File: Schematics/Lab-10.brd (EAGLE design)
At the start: 160 x 100 mm, 15 parts, among them IC1 OP350N, Q1 IRLD024

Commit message: Added LCD interface to the schematic
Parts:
- added C3: 0.33uf, EE445L:CAP100MIL
- added U$2: ST7735, EE445L:ST7735
- C2: value (none) -> 0.1uf
- R3, R4, R5, R6, R7: value (none) -> 10k
- R8: value (none) -> 200k
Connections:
- new net CS: U$1.J2-12, U$2.6
- new net D?C: U$1.J1-9, U$2.4
- new net MISO: U$1.J2-13, U$2.9
- new net MOSI: U$1.J1-8, U$2.7
- new net N$3: C3.2, Q1.P$3
- new net RST: U$1.J1-10, U$2.3
- new net SCK: U$1.J2-11, U$2.8
- net +3V3: now also U$2.10, U$2.2
- net GND: now also U$2.1
- net N$1: now also C3.1; no longer Q1.P$3
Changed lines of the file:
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@@
 <attribute name="VALUE" x="-61.976" y="-6.477" size="1.27" layer="27" ratio="10"/>
 </element>
-<element name="R3" library="EE445L" package="RES300MIL" value="" x="-59.69" y="-10.16" smashed="yes">
+<element name="R3" library="EE445L" package="RES300MIL" value="10k" x="-59.69" y="-10.16" smashed="yes">
 <attribute name="NAME" x="-62.23" y="-8.8646" size="0.9906" layer="25" ratio="10"/>
 <attribute name="VALUE" x="-61.3156" y="-10.6426" size="0.9906" layer="27" ratio="10"/>
 </element>
-<element name="R4" library="EE445L" package="RES300MIL" value="" x="-59.69" y="-15.24" smashed="yes">
+<element name="R4" library="EE445L" package="RES300MIL" value="10k" x="-59.69" y="-15.24" smashed="yes">
 <attribute name="NAME" x="-62.23" y="-13.9446" size="0.9906" layer="25" ratio="10"/>
 <attribute name="VALUE" x="-61.3156" y="-15.7226" size="0.9906" layer="27" ratio="10"/>
@@
 <attribute name="VALUE" x="-60.706" y="-22.225" size="1.27" layer="27" ratio="10"/>
 </element>
-<element name="R5" library="EE445L" package="RES200MIL" value="" x="-60.96" y="-29.21" smashed="yes">
+<element name="R5" library="EE445L" package="RES200MIL" value="10k" x="-60.96" y="-29.21" smashed="yes">
 <attribute name="NAME" x="-62.9666" y="-28.0416" size="0.9906" layer="25" ratio="10"/>
 <attribute name="VALUE" x="-63.0936" y="-31.5214" size="0.9906" layer="27" ratio="10"/>
 </element>
-<element name="R6" library="EE445L" package="RES200MIL" value="" x="-60.96" y="-33.02" smashed="yes">
+<element name="R6" library="EE445L" package="RES200MIL" value="10k" x="-60.96" y="-33.02" smashed="yes">
 <attribute name="NAME" x="-62.9666" y="-31.8516" size="0.9906" layer="25" ratio="10"/>
 <attribute name="VALUE" x="-63.0936" y="-35.3314" size="0.9906" layer="27" ratio="10"/>
 </element>
-<element name="R7" library="EE445L" package="RES200MIL" value="" x="-60.96" y="-36.83" smashed="yes">
+<element name="R7" library="EE445L" package="RES200MIL" value="10k" x="-60.96" y="-36.83" smashed="yes">
 <attribute name="NAME" x="-62.9666" y="-35.6616" size="0.9906" layer="25" ratio="10"/>
 <attribute name="VALUE" x="-63.0936" y="-39.1414" size="0.9906" layer="27" ratio="10"/>
 </element>
-<element name="R8" library="EE445L" package="RES200MIL" value="" x="-60.96" y="-40.64" smashed="yes">
+<element name="R8" library="EE445L" package="RES200MIL" value="200k" x="-60.96" y="-40.64" smashed="yes">
 <attribute name="NAME" x="-62.9666" y="-39.4716" size="0.9906" layer="25" ratio="10"/>
 <attribute name="VALUE" x="-63.0936" y="-42.9514" size="0.9906" layer="27" ratio="10"/>
 </element>
-<element name="C2" library="EE445L" package="CAP100MIL" value="" x="-62.23" y="-45.72" smashed="yes">
+<element name="C2" library="EE445L" package="CAP100MIL" value="0.1uf" x="-62.23" y="-45.72" smashed="yes">
 <attribute name="NAME" x="-64.008" y="-44.323" size="1.27" layer="25" ratio="10"/>
 <attribute name="VALUE" x="-64.008" y="-48.387" size="1.27" layer="27" ratio="10"/>
 </element>
+<element name="C3" library="EE445L" package="CAP100MIL" value="0.33uf" x="-62.23" y="-53.34" smashed="yes">
+<attribute name="NAME" x="-64.008" y="-51.943" size="1.27" layer="25" ratio="10"/>
+<attribute name="VALUE" x="-64.008" y="-56.007" size="1.27" layer="27" ratio="10"/>
+</element>
+<element name="U$2" library="EE445L" package="ST7735" value="ST7735" x="-62.23" y="-63.5" smashed="yes"/>
 </elements>
 <signals>
@@
 <contactref element="C2" pad="1"/>
 <contactref element="R5" pad="2"/>
+<contactref element="U$2" pad="1"/>
+<wire x1="-63.5" y1="-45.72" x2="-62.23" y2="-63.5" width="0" layer="19" extent="1-1"/>
 <wire x1="-58.42" y1="-29.21" x2="-63.5" y2="-45.72" width="0" layer="19" extent="1-1"/>
 <wire x1="-58.42" y1="-17.78" x2="-58.42" y2="-29.21" width="0" layer="19" extent="1-1"/>
@@
 <contactref element="C2" pad="2"/>
 <contactref element="R6" pad="1"/>
+<contactref element="U$2" pad="2"/>
+<contactref element="U$2" pad="10"/>
+<wire x1="-62.23" y1="-66.04" x2="-62.23" y2="-86.36" width="0" layer="19" extent="1-1"/>
+<wire x1="-60.96" y1="-45.72" x2="-62.23" y2="-66.04" width="0" layer="19" extent="1-1"/>
 <wire x1="-63.5" y1="-33.02" x2="-60.96" y2="-45.72" width="0" layer="19" extent="1-1"/>
 <wire x1="-53.34" y1="-25.4" x2="-63.5" y2="-33.02" width="0" layer="19" extent="1-1"/>
@@
 <signal name="N$1">
 <contactref element="R1" pad="2"/>
-<contactref element="Q1" pad="P$3"/>
-<wire x1="-49.53" y1="71.12" x2="-16.51" y2="71.12" width="0" layer="19" extent="1-1"/>
+<contactref element="C3" pad="1"/>
+<wire x1="-49.53" y1="71.12" x2="-63.5" y2="-53.34" width="0" layer="19" extent="1-1"/>
 </signal>
 <signal name="+5V">
@@
 <wire x1="-55.88" y1="-25.4" x2="-63.5" y2="-36.83" width="0" layer="19" extent="1-1"/>
 </signal>
+<signal name="N$3">
+<contactref element="Q1" pad="P$3"/>
+<contactref element="C3" pad="2"/>
+<wire x1="-16.51" y1="71.12" x2="-60.96" y2="-53.34" width="0" layer="19" extent="1-1"/>
+</signal>
+<signal name="RST">
+<contactref element="U$1" pad="J1-10"/>
+<contactref element="U$2" pad="3"/>
+<wire x1="-62.23" y1="13.97" x2="-62.23" y2="-68.58" width="0" layer="19" extent="1-1"/>
+</signal>
+<signal name="D?C">
+<contactref element="U$1" pad="J1-9"/>
+<contactref element="U$2" pad="4"/>
+<wire x1="-62.23" y1="16.51" x2="-62.23" y2="-71.12" width="0" layer="19" extent="1-1"/>
+</signal>
+<signal name="MOSI">
+<contactref element="U$1" pad="J1-8"/>
+<contactref element="U$2" pad="7"/>
+<wire x1="-62.23" y1="19.05" x2="-62.23" y2="-78.74" width="0" layer="19" extent="1-1"/>
+</signal>
+<signal name="MISO">
+<contactref element="U$1" pad="J2-13"/>
+<contactref element="U$2" pad="9"/>
+<wire x1="-16.51" y1="19.05" x2="-62.23" y2="-83.82" width="0" layer="19" extent="1-1"/>
+</signal>
+<signal name="CS">
+<contactref element="U$1" pad="J2-12"/>
+<contactref element="U$2" pad="6"/>
+<wire x1="-16.51" y1="16.51" x2="-62.23" y2="-76.2" width="0" layer="19" extent="1-1"/>
+</signal>
+<signal name="SCK">
+<contactref element="U$1" pad="J2-11"/>
+<contactref element="U$2" pad="8"/>
+<wire x1="-16.51" y1="13.97" x2="-62.23" y2="-81.28" width="0" layer="19" extent="1-1"/>
+</signal>
 </signals>

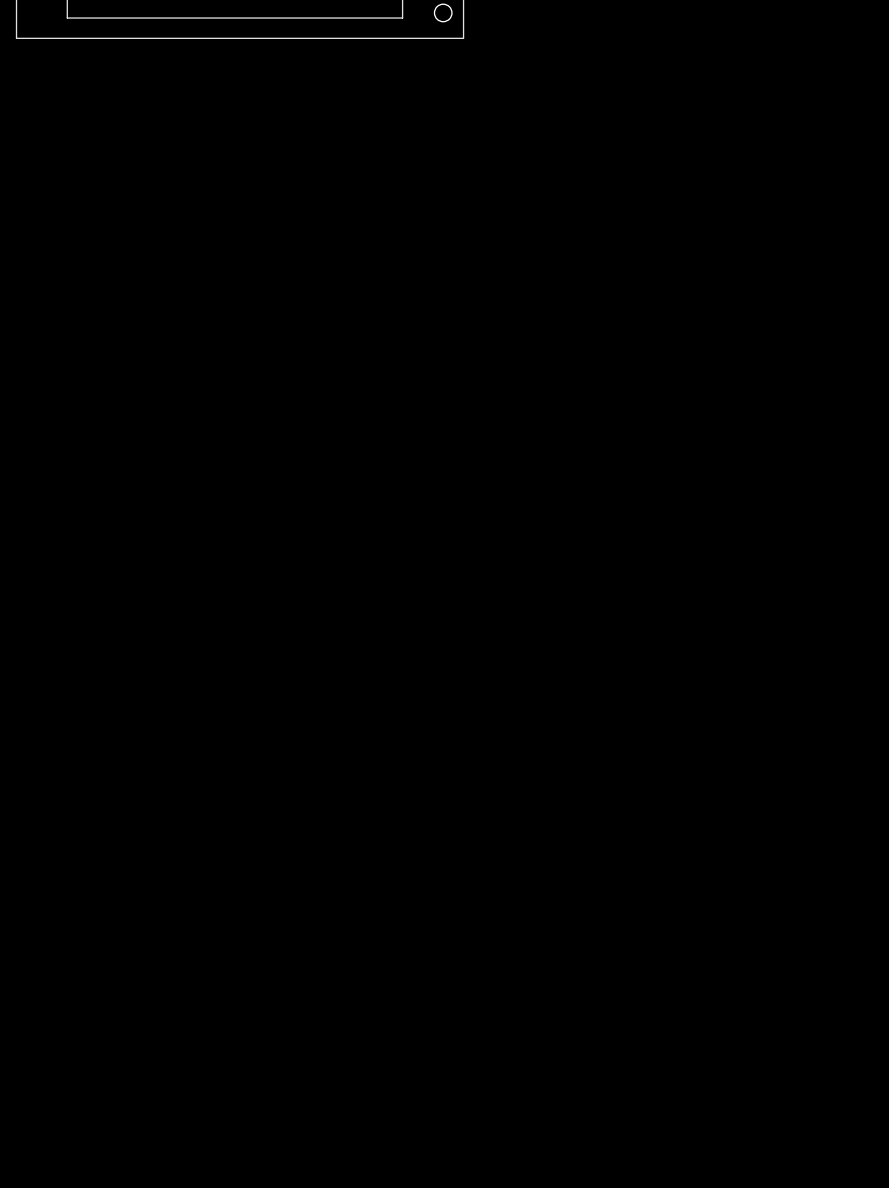
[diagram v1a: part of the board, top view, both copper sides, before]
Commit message: Added wifi block
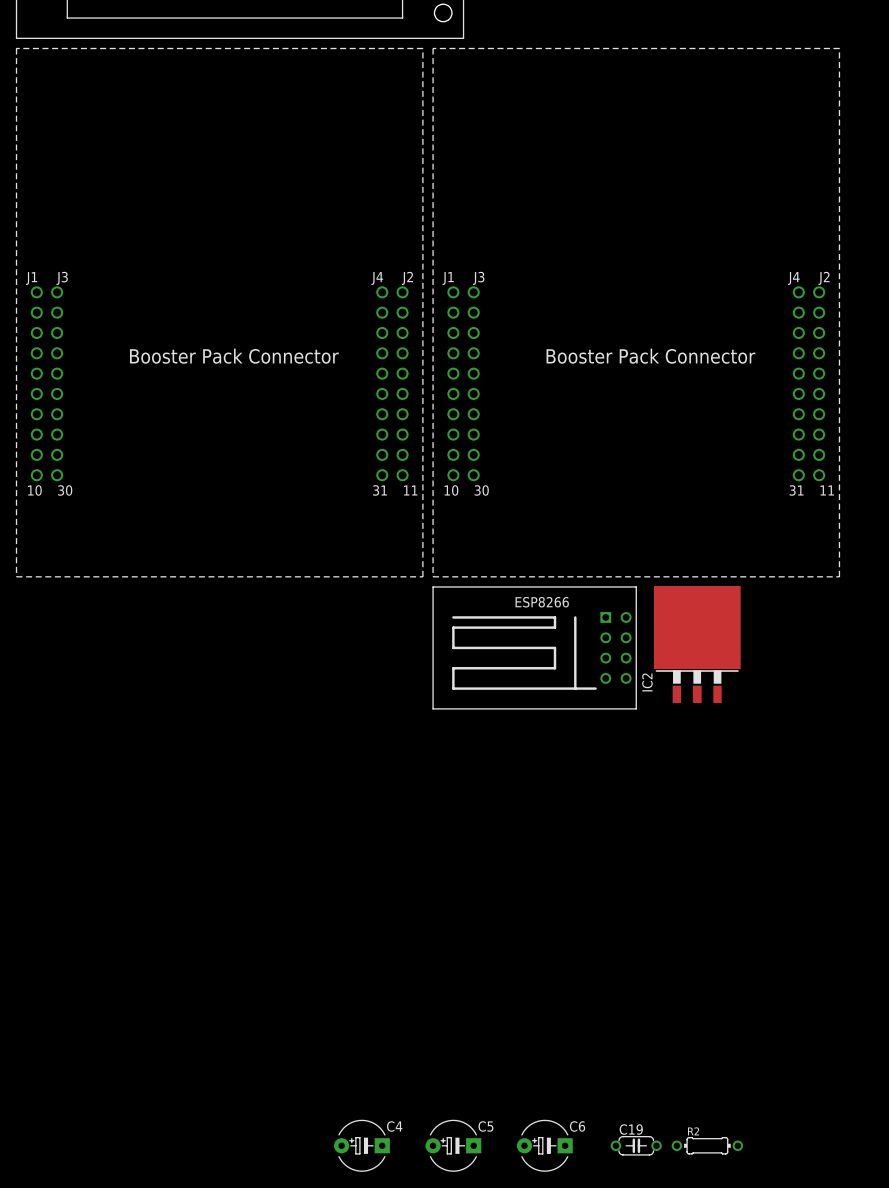
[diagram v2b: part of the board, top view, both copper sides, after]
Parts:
- added C19: 0.1uf, EE445L:CAP200MIL
- added C4, C5, C6: 4.7uf, EE445L:CAP200MILPOLARIZED
- added IC2: LM2937, linear:TO263-3
- added R2: 10K, EE445L:RES300MIL
- added U$3: ESP_8266, EE445L:ESP8266
- added U$4, U$5: TM4C_BP, EE445L:TM4C_BOOSTER_PACK
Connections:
- new net 3V3_ESP: C19.2, C4.+, C6.+, IC2.3, R2.2, U$3.CH_EN, U$3.VDD
- new net 5V0_USB: C5.+, IC2.1
- new net 8266_GPIO_0: R2.1, U$3.GPIO_0
- new net 8266_GPIO_2: U$3.GPIO_2, U$4.J2-18
- new net 8266_RX: U$3.RXD, U$4.J1-6
- new net 8266_TX: U$3.TXD, U$4.J1-5
- new net AIN_1: U$4.J3-28
- new net PD2: U$5.J3-25
- new net PD6: U$5.J4-33
- new net PD7: U$5.J4-32
- new net PE3: U$4.J3-29
- new net RSTB_8266: U$3.RST_B, U$4.J3-27
- new net SSI1_FS: U$5.J3-24
- new net SSI1_MOSI: U$5.J3-26
- new net SSI_SCK: U$5.J3-23
- net GND: now also C19.1, C4.-, C5.-, C6.-, IC2.2, U$3.GND
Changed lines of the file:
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@@
 </element>
 <element name="U$2" library="EE445L" package="ST7735" value="ST7735" x="-62.23" y="-63.5" smashed="yes"/>
+<element name="R2" library="EE445L" package="RES300MIL" value="10K" x="21.59" y="-231.14" smashed="yes">
+<attribute name="NAME" x="19.05" y="-229.8446" size="0.9906" layer="25" ratio="10"/>
+<attribute name="VALUE" x="19.9644" y="-231.6226" size="0.9906" layer="27" ratio="10"/>
+</element>
+<element name="C4" library="EE445L" package="CAP200MILPOLARIZED" value="4.7uf" x="-21.59" y="-231.14" smashed="yes">
+<attribute name="NAME" x="-18.542" y="-229.362" size="1.27" layer="25" ratio="10"/>
+<attribute name="VALUE" x="-18.542" y="-234.061" size="1.27" layer="27" ratio="10"/>
+</element>
+<element name="C19" library="EE445L" package="CAP200MIL" value="0.1uf" x="12.7" y="-231.14" smashed="yes">
+<attribute name="NAME" x="10.541" y="-229.743" size="1.27" layer="25" ratio="10"/>
+<attribute name="VALUE" x="10.541" y="-233.807" size="1.27" layer="27" ratio="10"/>
+</element>
+<element name="U$3" library="EE445L" package="ESP8266" value="ESP_8266" x="10.16" y="-168.91" smashed="yes"/>
+<element name="U$4" library="EE445L" package="TM4C_BOOSTER_PACK" value="TM4C_BP" x="-62.23" y="-147.32" smashed="yes"/>
+<element name="IC2" library="linear" library_urn="urn:adsk.eagle:library:262" package="TO263-3" package3d_urn="urn:adsk.eagle:package:16425/2" value="LM2937" x="20.32" y="-168.91" smashed="yes">
+<attribute name="NAME" x="14.732" y="-174.498" size="1.27" layer="25" rot="R90"/>
+<attribute name="POPULARITY" value="0" x="-124.46" y="-130.81" size="1.778" layer="27" display="off"/>
+<attribute name="VALUE" x="27.178" y="-174.498" size="1.27" layer="27" rot="R90"/>
+</element>
+<element name="C5" library="EE445L" package="CAP200MILPOLARIZED" value="4.7uf" x="-10.16" y="-231.14" smashed="yes">
+<attribute name="NAME" x="-7.112" y="-229.362" size="1.27" layer="25" ratio="10"/>
+<attribute name="VALUE" x="-7.112" y="-234.061" size="1.27" layer="27" ratio="10"/>
+</element>
+<element name="C6" library="EE445L" package="CAP200MILPOLARIZED" value="4.7uf" x="1.27" y="-231.14" smashed="yes">
+<attribute name="NAME" x="4.318" y="-229.362" size="1.27" layer="25" ratio="10"/>
+<attribute name="VALUE" x="4.318" y="-234.061" size="1.27" layer="27" ratio="10"/>
+</element>
+<element name="U$5" library="EE445L" package="TM4C_BOOSTER_PACK" value="TM4C_BP" x="-10.16" y="-147.32" smashed="yes"/>
 </elements>
 <signals>
@@
 <contactref element="R5" pad="2"/>
 <contactref element="U$2" pad="1"/>
+<contactref element="C4" pad="-"/>
+<contactref element="C19" pad="1"/>
+<contactref element="U$3" pad="GND"/>
+<contactref element="IC2" pad="2"/>
+<contactref element="C5" pad="-"/>
+<contactref element="C6" pad="-"/>
+<wire x1="-7.62" y1="-231.14" x2="-19.05" y2="-231.14" width="0" layer="19" extent="1-1"/>
+<wire x1="3.81" y1="-231.14" x2="-7.62" y2="-231.14" width="0" layer="19" extent="1-1"/>
+<wire x1="10.16" y1="-231.14" x2="3.81" y2="-231.14" width="0" layer="19" extent="1-1"/>
+<wire x1="20.32" y1="-174.7012" x2="10.16" y2="-231.14" width="0" layer="19" extent="1-1"/>
+<wire x1="8.89" y1="-172.72" x2="20.32" y2="-174.7012" width="0" layer="19" extent="1-1"/>
+<wire x1="-62.23" y1="-63.5" x2="8.89" y2="-172.72" width="0" layer="19" extent="1-1"/>
 <wire x1="-63.5" y1="-45.72" x2="-62.23" y2="-63.5" width="0" layer="19" extent="1-1"/>
 <wire x1="-58.42" y1="-29.21" x2="-63.5" y2="-45.72" width="0" layer="19" extent="1-1"/>
@@
 <wire x1="-16.51" y1="13.97" x2="-62.23" y2="-81.28" width="0" layer="19" extent="1-1"/>
 </signal>
+<signal name="8266_RX">
+<contactref element="U$3" pad="RXD"/>
+<contactref element="U$4" pad="J1-6"/>
+<wire x1="8.89" y1="-165.1" x2="-62.23" y2="-137.16" width="0" layer="19" extent="1-1"/>
+</signal>
+<signal name="8266_TX">
+<contactref element="U$3" pad="TXD"/>
+<contactref element="U$4" pad="J1-5"/>
+<wire x1="11.43" y1="-172.72" x2="-62.23" y2="-134.62" width="0" layer="19" extent="1-1"/>
+</signal>
+<signal name="AIN_1">
+<contactref element="U$4" pad="J3-28"/>
+</signal>
+<signal name="RSTB_8266">
+<contactref element="U$3" pad="RST_B"/>
+<contactref element="U$4" pad="J3-27"/>
+<wire x1="11.43" y1="-167.64" x2="-59.69" y2="-139.7" width="0" layer="19" extent="1-1"/>
+</signal>
+<signal name="8266_GPIO_2">
+<contactref element="U$3" pad="GPIO_2"/>
+<contactref element="U$4" pad="J2-18"/>
+<wire x1="-16.51" y1="-129.54" x2="8.89" y2="-170.18" width="0" layer="19" extent="1-1"/>
+</signal>
+<signal name="8266_GPIO_0">
+<contactref element="R2" pad="1"/>
+<contactref element="U$3" pad="GPIO_0"/>
+<wire x1="8.89" y1="-167.64" x2="17.78" y2="-231.14" width="0" layer="19" extent="1-1"/>
+</signal>
+<signal name="PE3">
+<contactref element="U$4" pad="J3-29"/>
+</signal>
+<signal name="5V0_USB">
+<contactref element="IC2" pad="1"/>
+<contactref element="C5" pad="+"/>
+<wire x1="17.78" y1="-174.7012" x2="-12.7" y2="-231.14" width="0" layer="19" extent="1-1"/>
+</signal>
+<signal name="3V3_ESP">
+<contactref element="IC2" pad="3"/>
+<contactref element="C6" pad="+"/>
+<contactref element="R2" pad="2"/>
+<contactref element="C4" pad="+"/>
+<contactref element="C19" pad="2"/>
+<contactref element="U$3" pad="CH_EN"/>
+<contactref element="U$3" pad="VDD"/>
+<wire x1="15.24" y1="-231.14" x2="-1.27" y2="-231.14" width="0" layer="19" extent="1-1"/>
+<wire x1="25.4" y1="-231.14" x2="15.24" y2="-231.14" width="0" layer="19" extent="1-1"/>
+<wire x1="-24.13" y1="-231.14" x2="-1.27" y2="-231.14" width="0" layer="19" extent="1-1"/>
+<wire x1="22.86" y1="-174.7012" x2="25.4" y2="-231.14" width="0" layer="19" extent="1-1"/>
+<wire x1="11.43" y1="-170.18" x2="22.86" y2="-174.7012" width="0" layer="19" extent="1-1"/>
+<wire x1="11.43" y1="-165.1" x2="11.43" y2="-170.18" width="0" layer="19" extent="1-1"/>
+</signal>
+<signal name="PD7">
+<contactref element="U$5" pad="J4-32"/>
+</signal>
+<signal name="PD6">
+<contactref element="U$5" pad="J4-33"/>
+</signal>
+<signal name="SSI1_MOSI">
+<contactref element="U$5" pad="J3-26"/>
+</signal>
+<signal name="PD2">
+<contactref element="U$5" pad="J3-25"/>
+</signal>
+<signal name="SSI1_FS">
+<contactref element="U$5" pad="J3-24"/>
+</signal>
+<signal name="SSI_SCK">
+<contactref element="U$5" pad="J3-23"/>
+</signal>
 </signals>
 <mfgpreviewcolors>
@@
 </board>
 </drawing>
+<compatibility>
+<note version="8.2" severity="warning">
+Since Version 8.2, EAGLE supports online libraries. The ids
+of those online libraries will not be understood (or retained)
+with this version.
+</note>
+<note version="8.3" severity="warning">
+Since Version 8.3, EAGLE supports URNs for individual library
+assets (packages, symbols, and devices). The URNs of those assets
+will not be understood (or retained) with this version.
+</note>
+<note version="8.3" severity="warning">
+Since Version 8.3, EAGLE supports the association of 3D packages
+with devices in libraries, schematics, and board files. Those 3D
+packages will not be understood (or retained) with this version.
+</note>
+</compatibility>
 </eagle>
